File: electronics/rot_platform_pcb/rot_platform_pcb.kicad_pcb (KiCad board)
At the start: 2 copper layers, 67.3 x 58.4 mm, 17 parts, among them J1 Motor_out, J2 Heating_conn, J3 Pump_conn, J4 Encoder_conn, J5 UART_Debug, J6 I2C_conn, J7 Endstop, J9 Power, Q1 IRLZ44N, Q2 IRLZ44N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

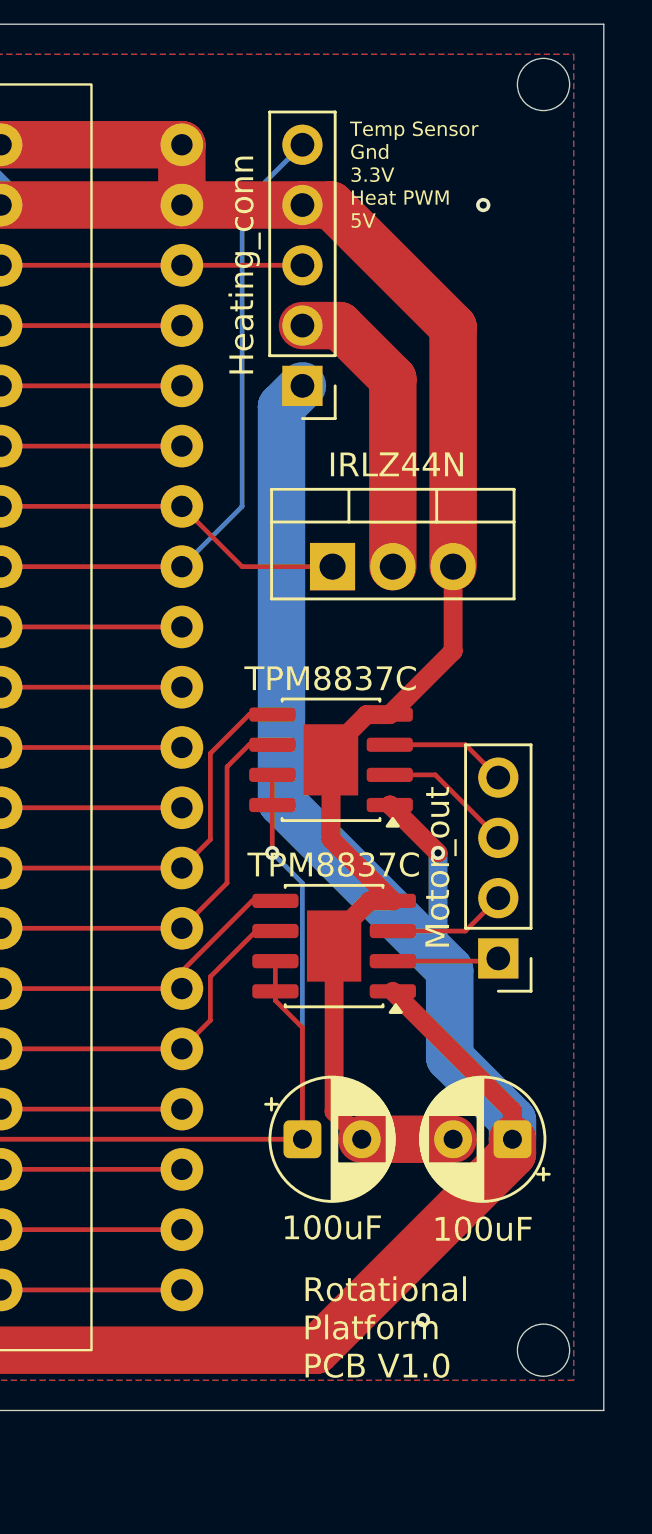
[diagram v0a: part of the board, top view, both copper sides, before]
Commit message: update rotational stage PCB to V1.1
Fixed a few issues in V1.0
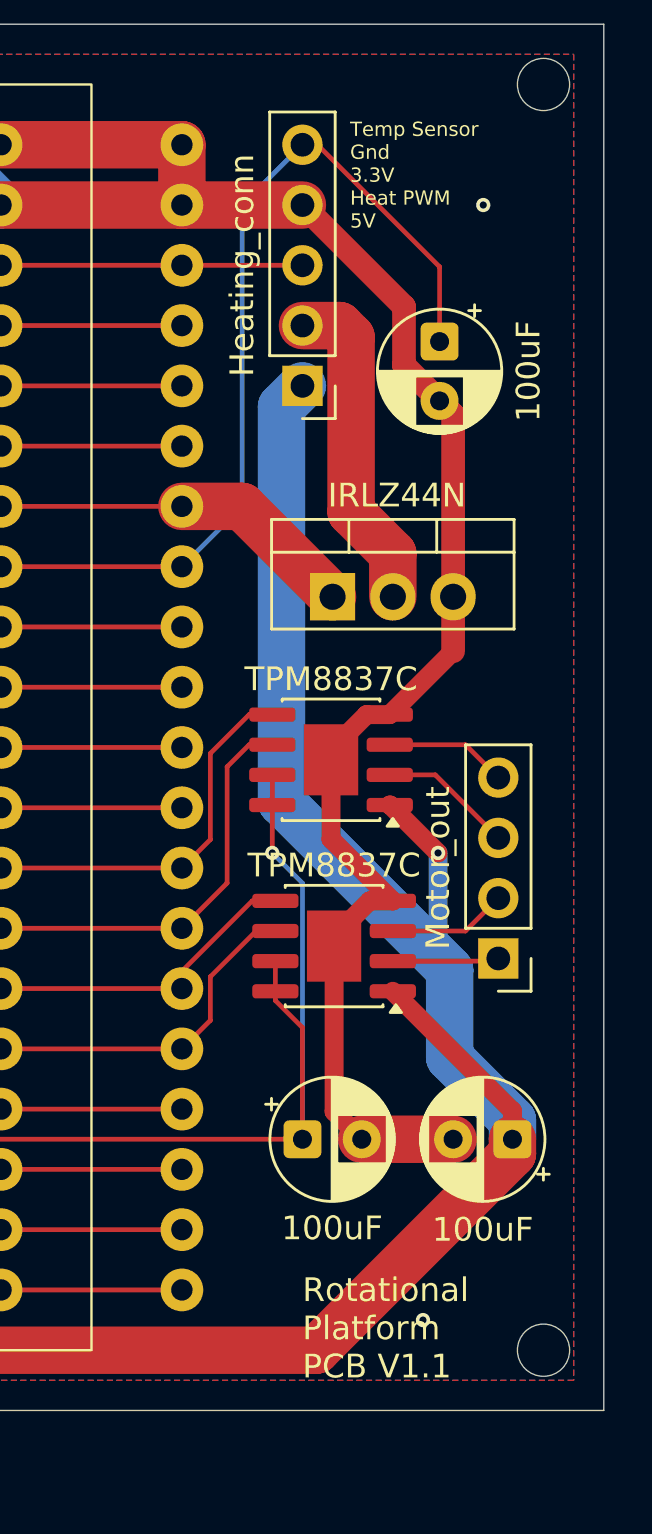
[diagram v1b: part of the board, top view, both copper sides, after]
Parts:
- added C4: 100uF, Capacitor_THT:CP_Radial_D5.0mm_P2.50mm, F.Cu at (170.9, 59.1)
- moved Q1 1.27 mm to (166.4, 69.8)
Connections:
- net Net-(J2-Pin_5) renamed /Temp_in
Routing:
- net /Temp_in: track 27.5 -> 38.6 mm
- net /Heating_out: track 12.7 -> 13.9 mm
- net GND: track 155.5 -> 154.8 mm
- net Net-(Q1-G): track 15.0 -> 15.5 mm
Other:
- board text added: "Rotational Platform PCB V1.1"
- board text removed: "Rotational Platform PCB V1.0"
